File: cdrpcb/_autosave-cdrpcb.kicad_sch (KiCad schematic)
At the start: 42 parts, among them J1 Conn_02x04_Odd_Even, J2 Conn_01x03, J3 Conn_01x03, J4 Conn_01x03, J5 Conn_01x03, J6 Conn_01x03, J7 Conn_01x06, J8 Conn_01x05, J9 Conn_01x03, SW1 SW_Push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

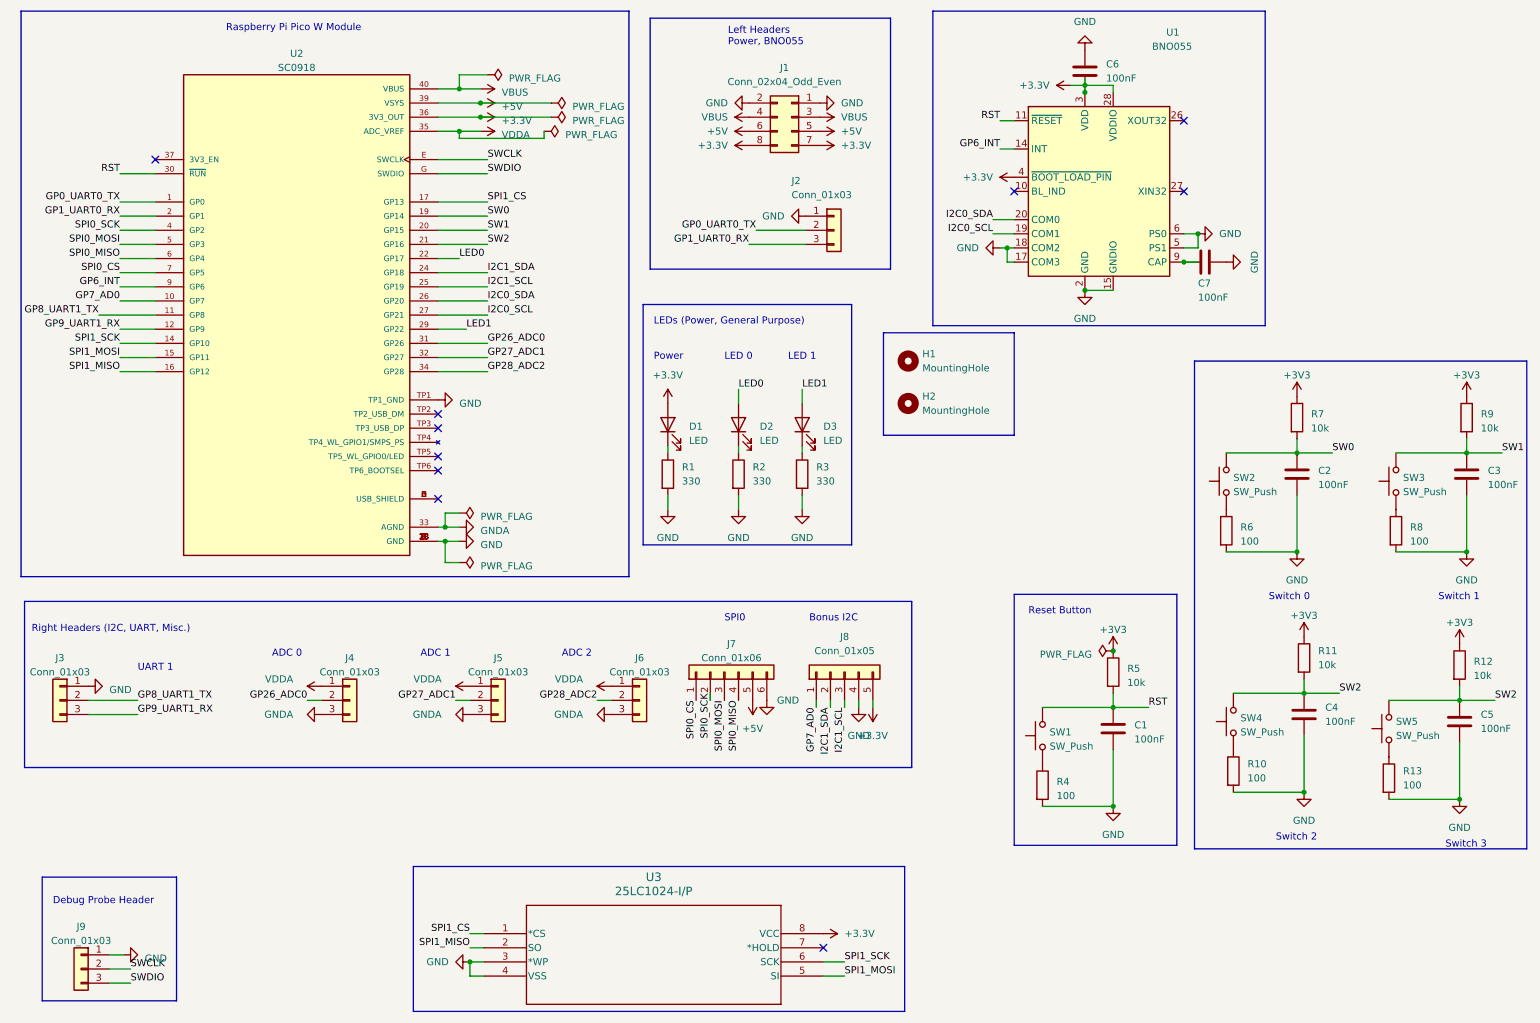
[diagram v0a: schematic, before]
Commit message: update cdrpcb
bno055 footprints
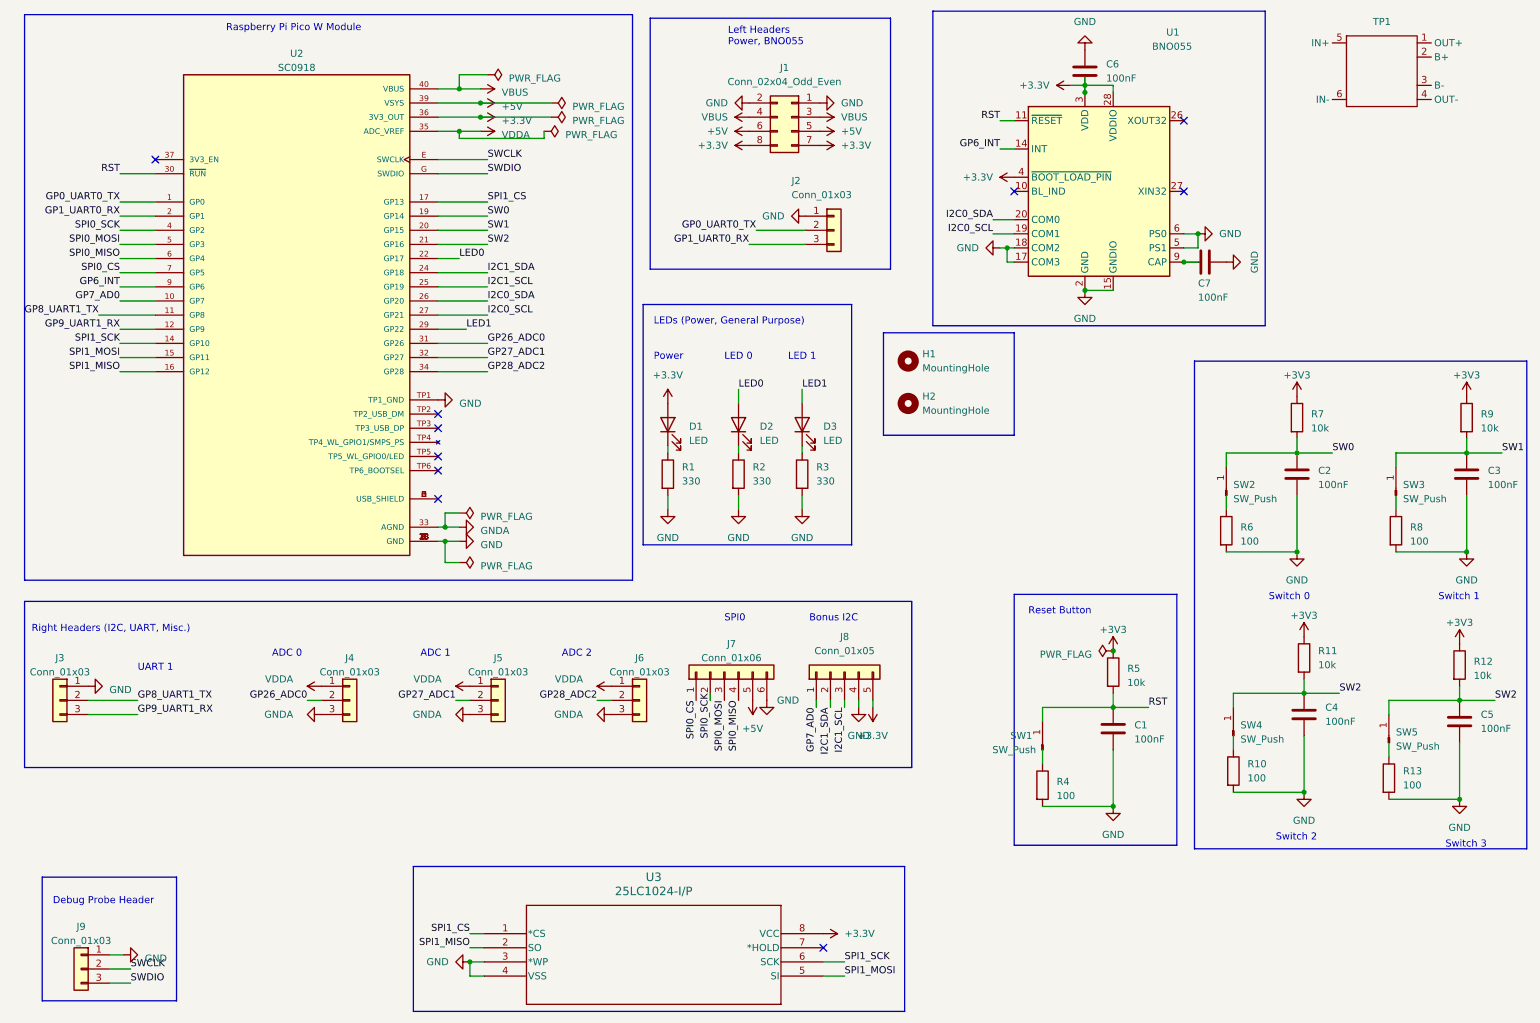
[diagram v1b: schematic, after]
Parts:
- removed SW1, SW2, SW3, SW4, SW5: SW_Push, Button_Switch_THT:SW_PUSH_6mm, symbol Switch:SW_Push
- added SW1, SW3: SW_Push, Connector_PinHeader_2.54mm:PinHeader_1x01_P2.54mm_Vertical, symbol Connector:Conn_01x01_Pin
- added SW2, SW4, SW5: SW_Push, Connector_PinHeader_2.54mm:PinHeader_1x02_P2.54mm_Vertical, symbol Connector:Conn_01x01_Pin
- added TP1: ~, TP4056:TP4056-18650, symbol TP4056:TP4056
- U1: footprint Package_LGA:LGA-28_5.2x3.8mm_P0.5mm -> Adafruit BNO055:MOUNTINGHOLE_2.5_PLATED_THICK
- U2: footprint SC0918:MODULE_SC0918 -> RP2040_SC0918:MODULE_SC0918
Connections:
- net RST: now also SW1.1 (Pin_1)
- net SW0: now also SW2.1 (Pin_1)
- net SW1: now also SW3.1 (Pin_1)
- net SW2: now also SW4.1 (Pin_1), SW5.1 (Pin_1)

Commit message: cdrpcb3
Started routing
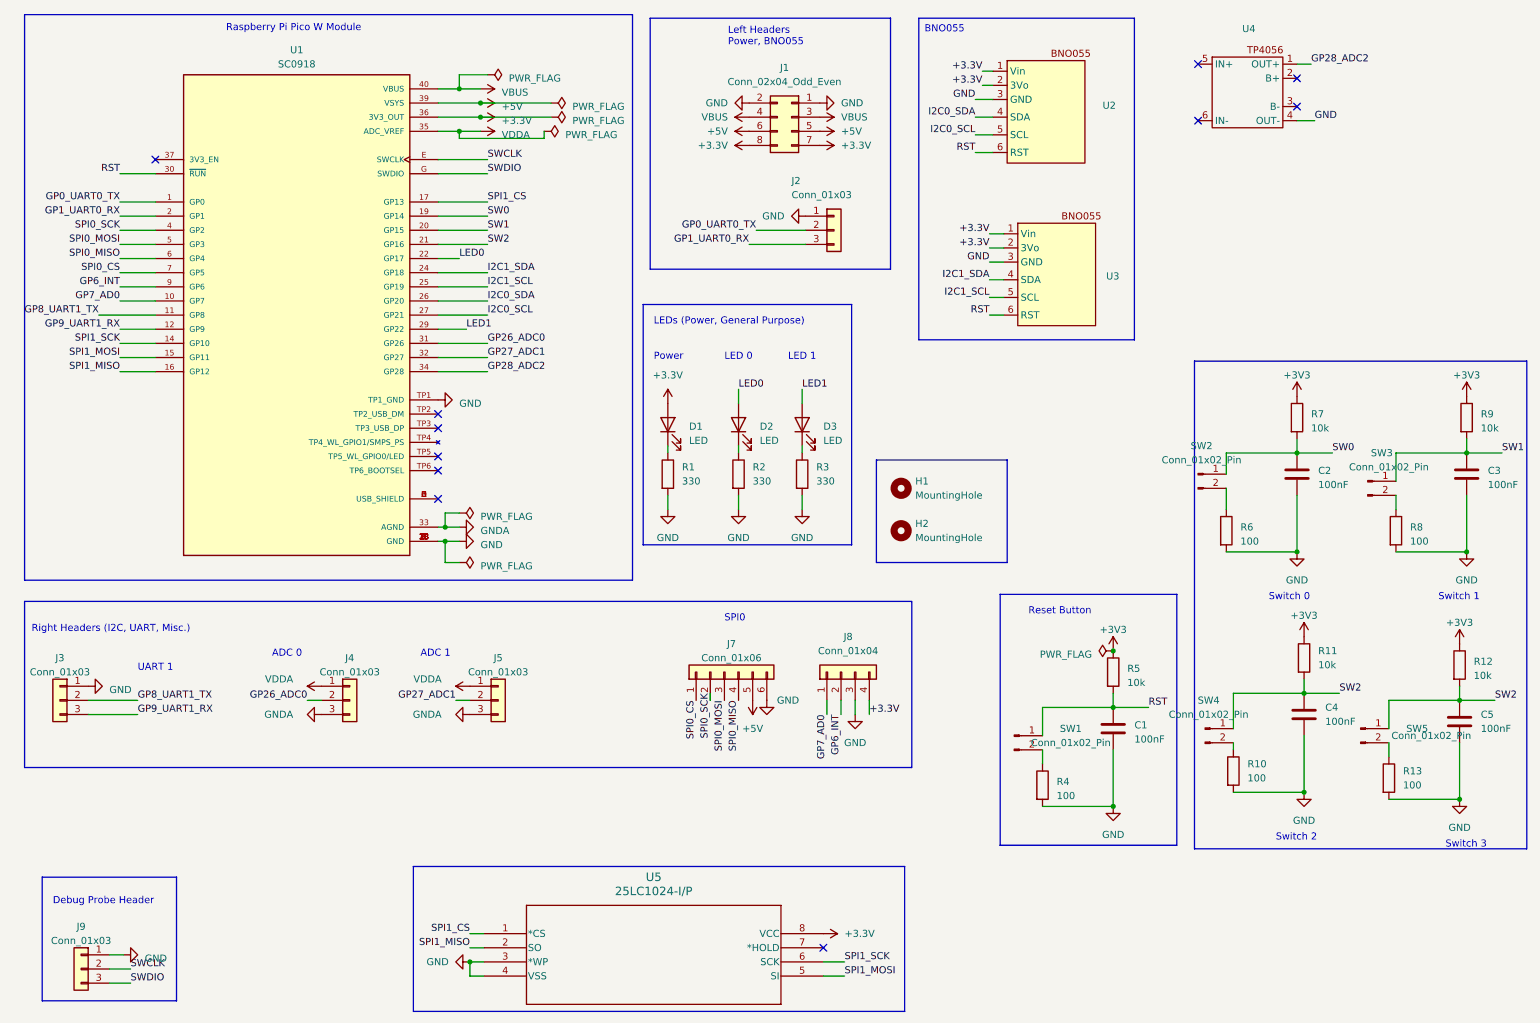
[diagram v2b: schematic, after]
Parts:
- removed C6, C7: 100nF, Capacitor_THT:CP_Radial_D4.0mm_P1.50mm, symbol Device:C
- removed J6: Conn_01x03, Connector_PinHeader_2.54mm:PinHeader_1x03_P2.54mm_Vertical, symbol Connector_Generic:Conn_01x03
- removed J8: Conn_01x05, Connector_PinHeader_2.54mm:PinHeader_1x05_P2.54mm_Vertical, symbol Connector_Generic:Conn_01x05
- removed SW1, SW3: SW_Push, Connector_PinHeader_2.54mm:PinHeader_1x01_P2.54mm_Vertical, symbol Connector:Conn_01x01_Pin
- removed SW2, SW4, SW5: SW_Push, Connector_PinHeader_2.54mm:PinHeader_1x02_P2.54mm_Vertical, symbol Connector:Conn_01x01_Pin
- removed TP1: ~, TP4056:TP4056-18650, symbol TP4056:TP4056
- removed U1: BNO055, Adafruit BNO055:MOUNTINGHOLE_2.5_PLATED_THICK, symbol Sensor_Motion:BNO055
- added J8: Conn_01x04, Connector_PinHeader_2.54mm:PinHeader_1x04_P2.54mm_Vertical, symbol Connector_Generic:Conn_01x04
- added SW1, SW2, SW3, SW4, SW5: Conn_01x02_Pin, Connector_PinHeader_2.54mm:PinHeader_1x02_P2.54mm_Vertical, symbol Connector:Conn_01x02_Pin
- added U2, U3: ~, Library:BNO055_Breakout, symbol Adafruit BNO055-eagle-import:BNO055_Breakout
- added U4: ~, TP4056:TP4056-18650, symbol TP4056:TP4056
- renumbered U2 to U1, U3 to U5
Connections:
- net +3.3V: now also J8.4 (Pin_4), U2.1 (Vin), U2.2 (3Vo), U3.1 (Vin), U3.2 (3Vo)
- net GND: now also J8.3 (Pin_3), U2.3 (GND), U3.3 (GND), U4.4 (OUT-)
- net GP28_ADC2: now also U4.1 (OUT+)
- net GP6_INT: now also J8.2 (Pin_2)
- net GP7_AD0: now also J8.1 (Pin_1)
- net I2C0_SCL: now also U2.5 (SCL)
- net I2C0_SDA: now also U2.4 (SDA)
- net I2C1_SCL: now also U3.5 (SCL)
- net I2C1_SDA: now also U3.4 (SDA)
- net RST: now also SW1.1 (Pin_1), U2.6 (RST), U3.6 (RST)
- net SW0: now also SW2.1 (Pin_1)
- net SW1: now also SW3.1 (Pin_1)
- net SW2: now also SW4.1 (Pin_1), SW5.1 (Pin_1)
- net at R13.1: now also SW5.2 (Pin_2)
- net at R4.1: now also SW1.2 (Pin_2)
- net at R10.1: now also SW4.2 (Pin_2)
- net at R8.1: now also SW3.2 (Pin_2)
- net at R6.1: now also SW2.2 (Pin_2)
- no-connect marks 10 -> 11
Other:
- note removed: "ADC 2"
- note removed: "Bonus I2C"
- moved on the sheet: H1, H2
